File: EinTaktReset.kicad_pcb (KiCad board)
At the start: 2 copper layers, 58 parts, among them IC1 74LS624, J1 3PinTerminalBlocktg, J2 3PinTerminalBlocktg, J3 2PinTerminalBlocktg, J4 3PinTerminalBlocktg, J5 2PinTerminalBlocktg, P1 CONN_02X10, P4 CONN_02X10, SW1 SPST, SW10 SPST, SW11 SPST, SW12 SPST, SW13 SPST, SW2 SWITCH_INV, SW3 SPST, SW4 SPST, SW5 SPST, SW6 SWITCH_INV, SW7 SPST, SW8 SPST, SW9 SPST, U1 74LS132, U2 74540En, U3 74HCT541_PWR, U4 74LS32, U5 74LS00

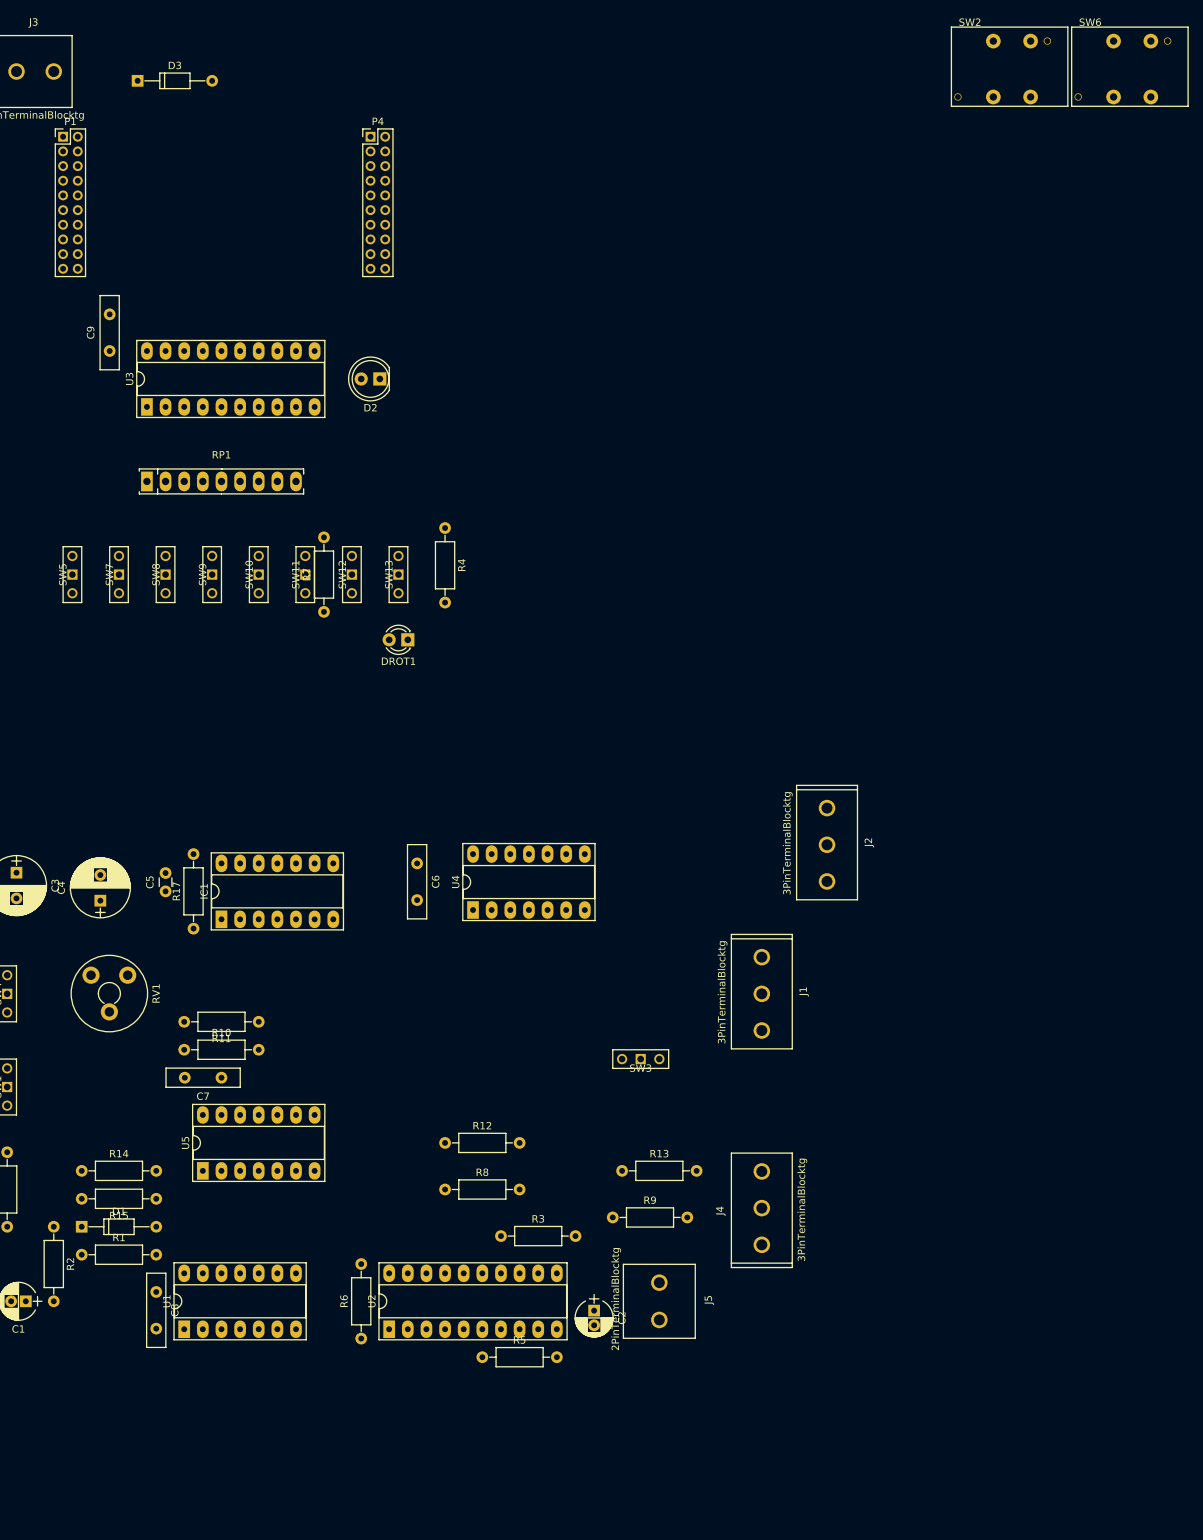
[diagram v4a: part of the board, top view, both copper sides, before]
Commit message: neuer footprint für switch
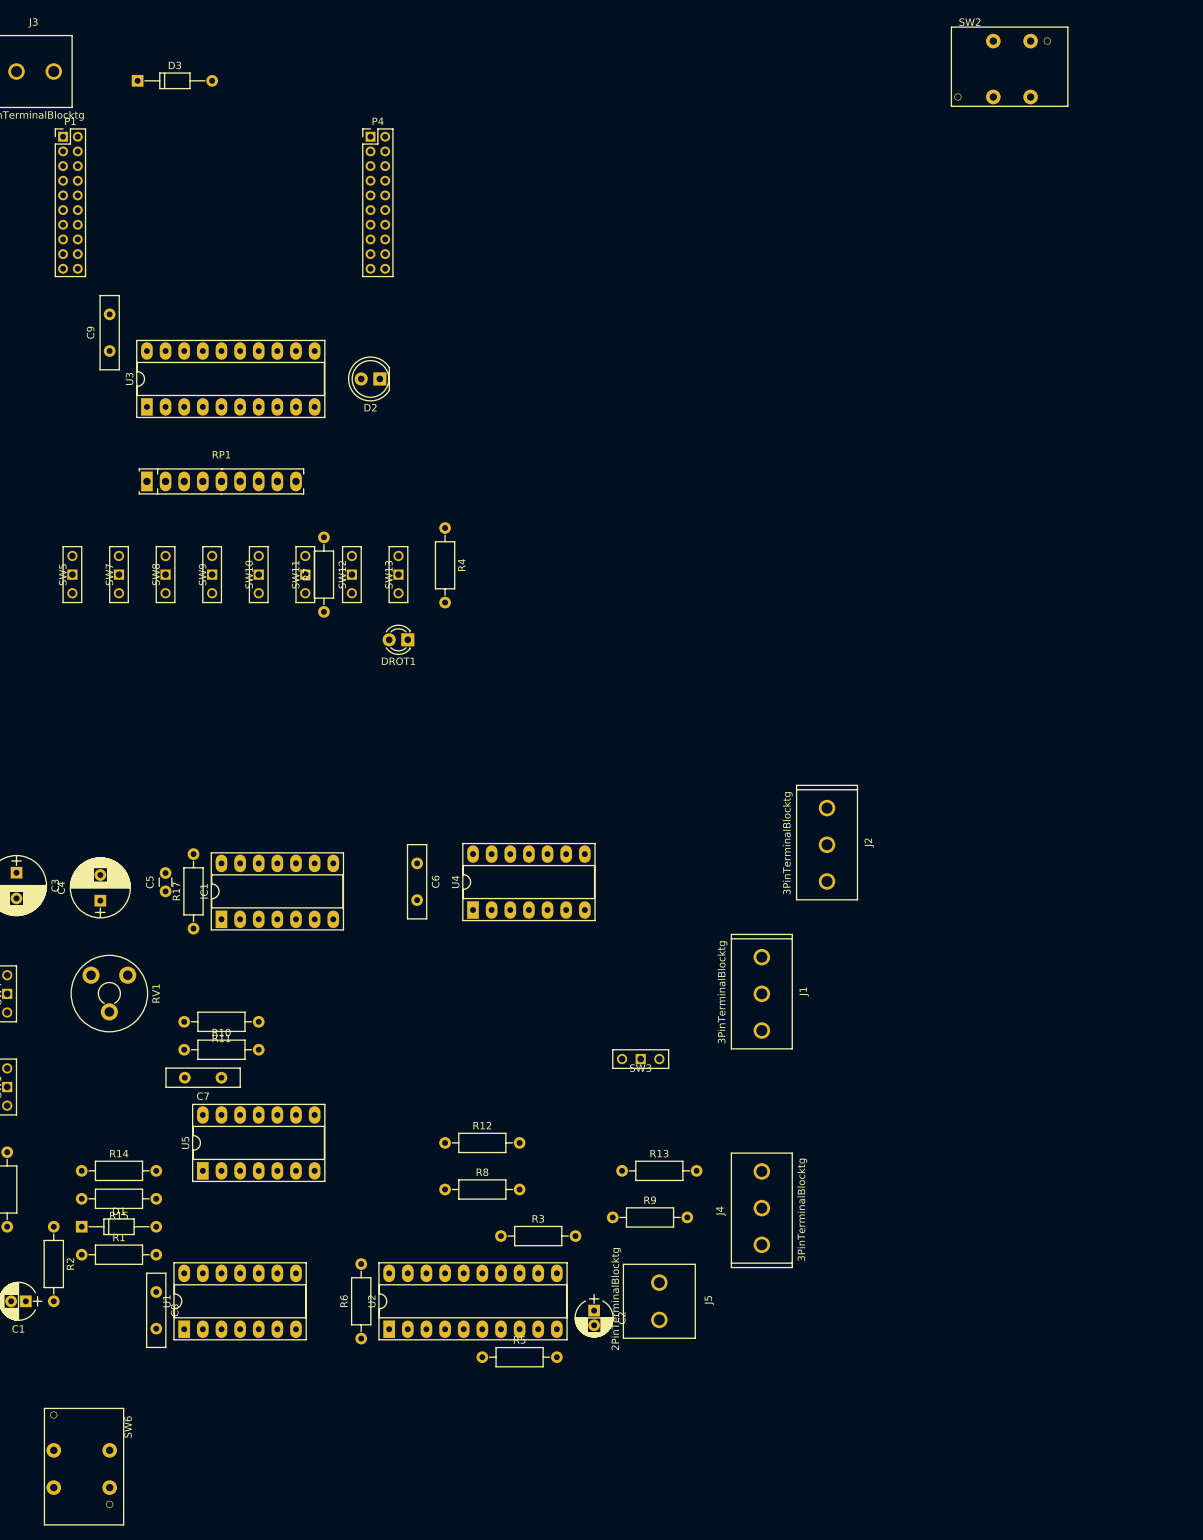
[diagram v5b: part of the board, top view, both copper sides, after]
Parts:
- moved SW6 243.0 mm to (29.2, 210.8), turned to 270 degrees
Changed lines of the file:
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@@
   )
   (module tg_foodprint:SW_PUSH_LCD_E3_SAxxxx_tg (layer F.Cu)
-    (at 171.139157 13.631782)
+    (at 29.21 210.82 270)
     (descr "Switch with LCD screen E3 SAxxxx")
     (tags "switch normally-open pushbutton push-button LCD")
-    (fp_text reference SW6 (at -8.255 -2.54) (layer F.SilkS)
+    (fp_text reference SW6 (at -8.255 -2.54 270) (layer F.SilkS)
       (effects (font (size 1 1) (thickness 0.15)))
     )
@@
       (effects (font (size 1 1) (thickness 0.15)))
     )
-    (fp_text user %R (at -7.5 3.81) (layer F.Fab)
+    (fp_text user %R (at -7.5 3.81 270) (layer F.Fab)
       (effects (font (size 1 1) (thickness 0.15)))
     )
@@
     (fp_line (start 5.08 -1.905) (end -10.795 -1.905) (layer F.Fab) (width 0.1))
     (fp_line (start 5.08 -1.905) (end 5.08 8.89) (layer F.Fab) (width 0.1))
-    (pad 2 thru_hole circle (at 0 7.62) (size 2 2) (drill 1) (layers *.Cu *.Mask)
+    (pad 2 thru_hole circle (at 0 7.62 270) (size 2 2) (drill 1) (layers *.Cu *.Mask)
       (net 11 auto))
-    (pad 0 thru_hole circle (at -5.08 7.62) (size 2 2) (drill 1) (layers *.Cu *.Mask))
-    (pad 1 thru_hole circle (at 0 0) (size 2 2) (drill 1) (layers *.Cu *.Mask)
+    (pad 0 thru_hole circle (at -5.08 7.62 270) (size 2 2) (drill 1) (layers *.Cu *.Mask))
+    (pad 1 thru_hole circle (at 0 0 270) (size 2 2) (drill 1) (layers *.Cu *.Mask)
       (net 12 GND))
-    (pad 5 thru_hole circle (at -9.906 7.62) (size 1 1) (drill 0.8) (layers *.Cu *.Mask))
-    (pad 6 thru_hole circle (at 2.286 0) (size 1 1) (drill 0.8) (layers *.Cu *.Mask))
-    (pad 0 thru_hole circle (at -5.08 0) (size 2 2) (drill 1) (layers *.Cu *.Mask))
+    (pad 5 thru_hole circle (at -9.906 7.62 270) (size 1 1) (drill 0.8) (layers *.Cu *.Mask))
+    (pad 6 thru_hole circle (at 2.286 0 270) (size 1 1) (drill 0.8) (layers *.Cu *.Mask))
+    (pad 0 thru_hole circle (at -5.08 0 270) (size 2 2) (drill 1) (layers *.Cu *.Mask))
     (model ${KISYS3DMOD}/Buttons_Switches_THT.3dshapes/SW_PUSH_LCD_E3_SAxxxx.wrl
       (at (xyz 0 0 0))

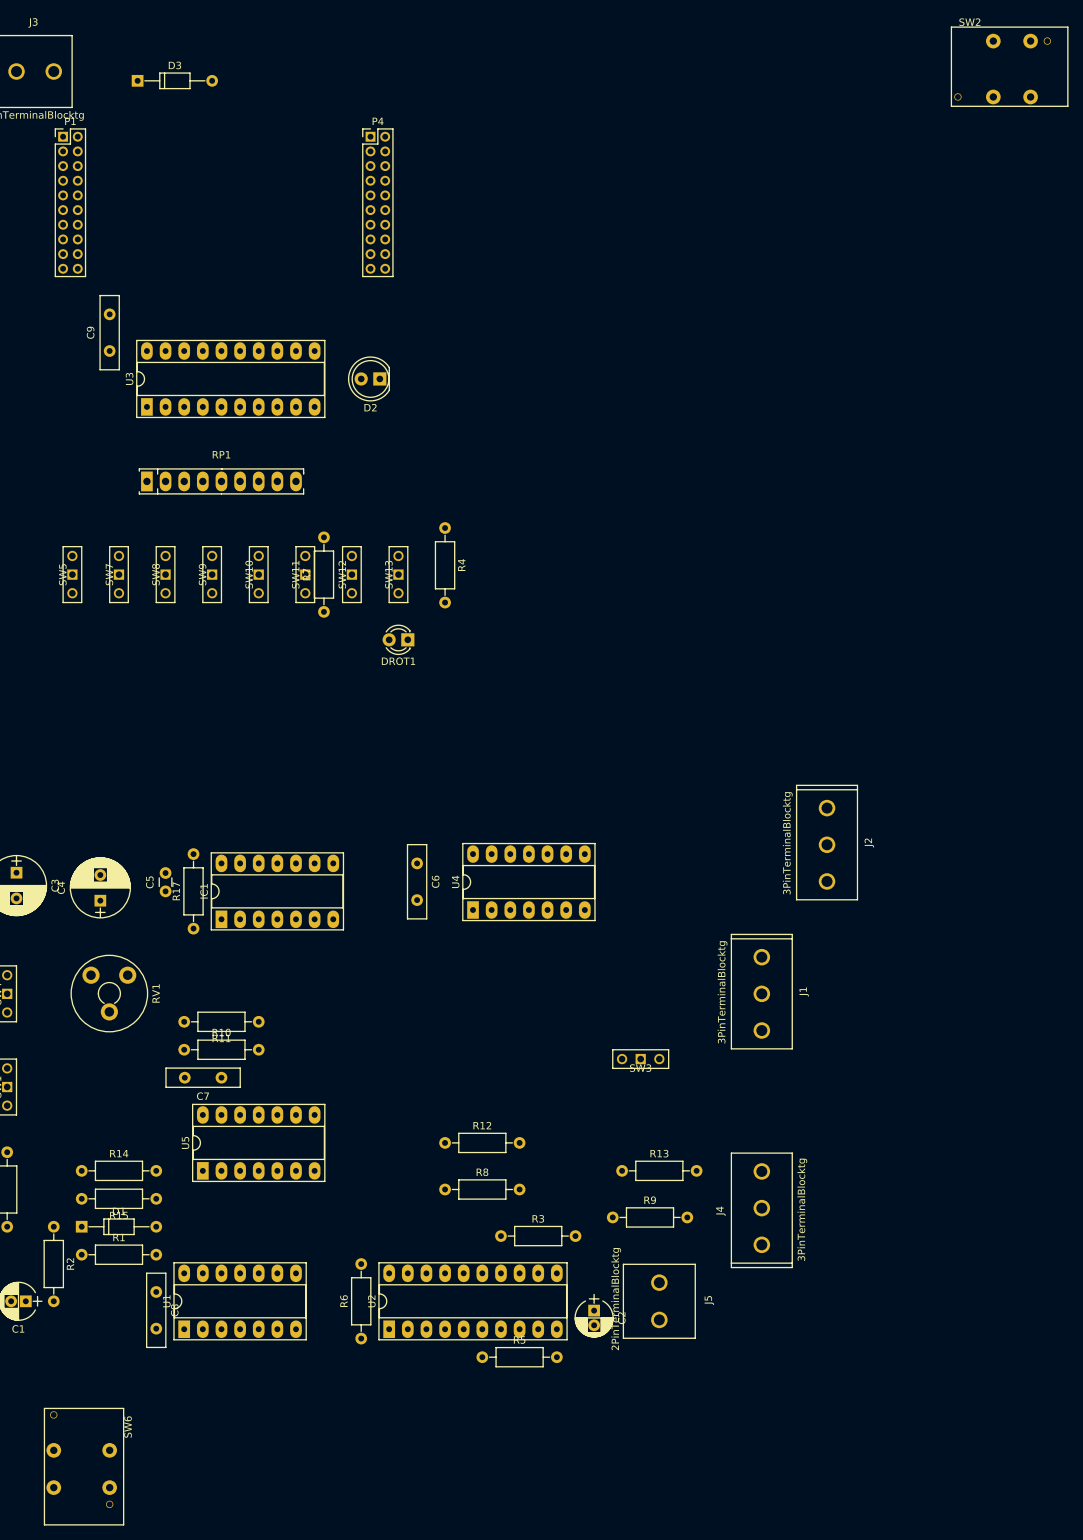
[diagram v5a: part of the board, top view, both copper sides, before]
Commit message: Resistoren angepasst, switches geändert, sw6 braucht noch anpassung
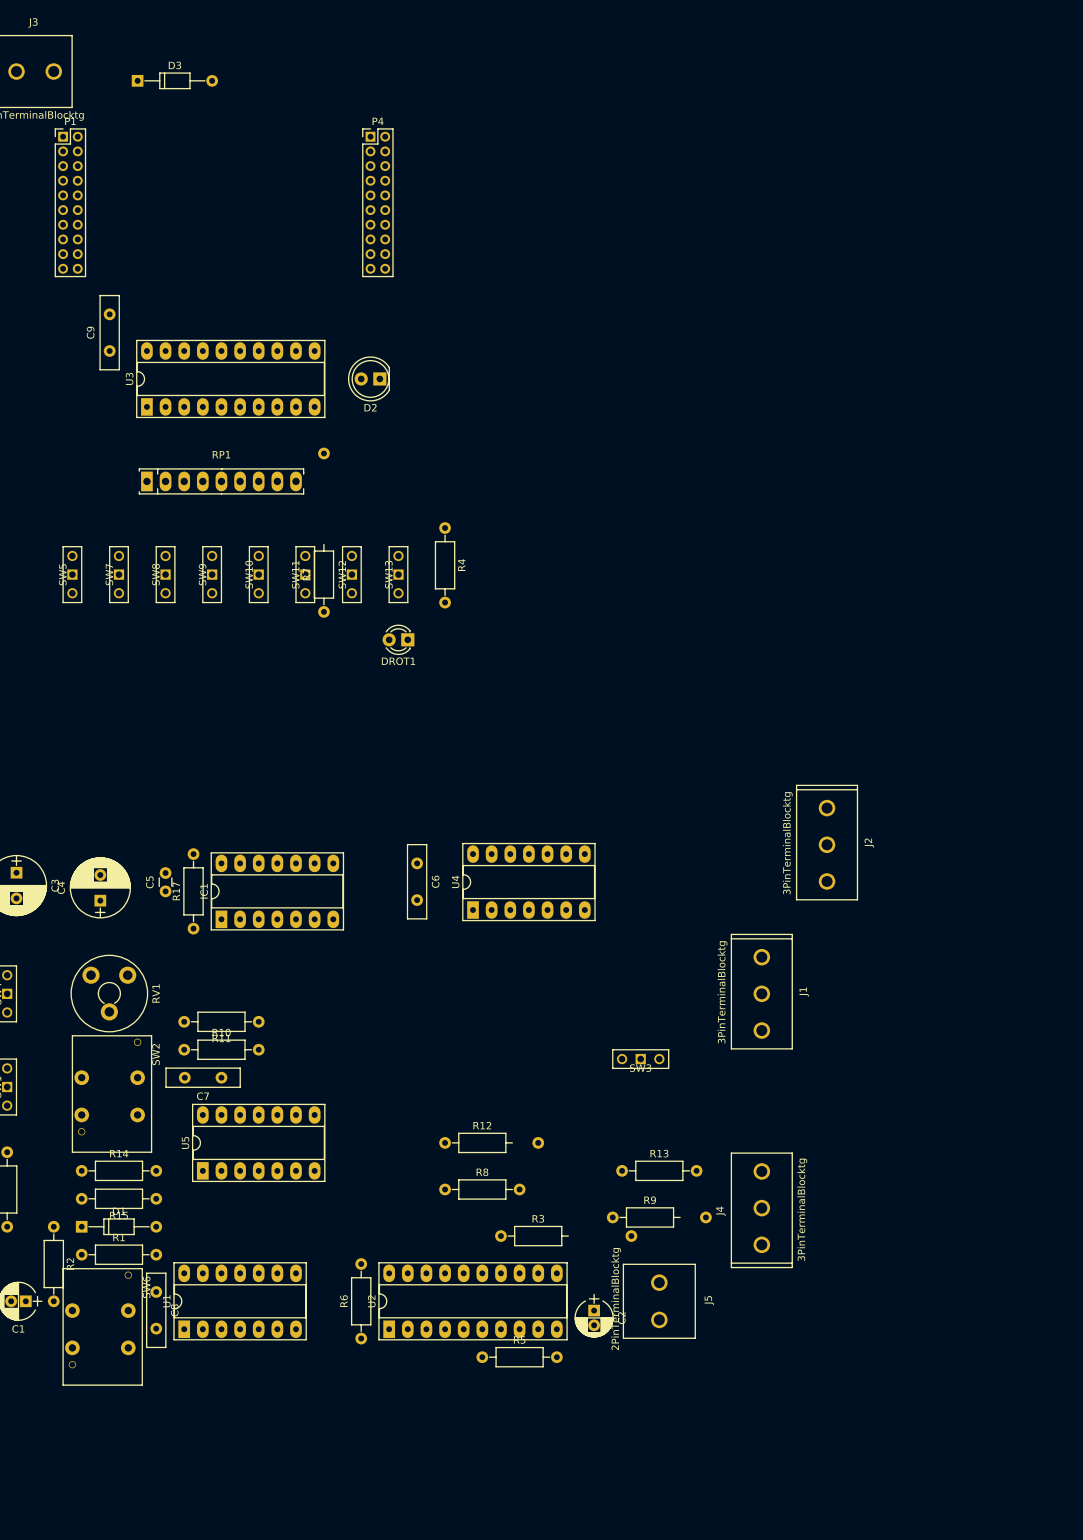
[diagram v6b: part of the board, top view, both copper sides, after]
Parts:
- R12, R9: footprint Resistors_ThroughHole:R_Axial_DIN0207_L6.3mm_D2.5mm_P10.16mm_Horizontal -> tg_foodprint:R_Axial_DIN0207_L6.3mm_D2.5mm_P12.7mm_Horizontaltg
- R3: footprint Resistors_ThroughHole:R_Axial_DIN0207_L6.3mm_D2.5mm_P10.16mm_Horizontal -> tg_foodprint:R_Axial_DIN0207_L6.3mm_D2.5mm_P17.7mm_Horizontaltg
- R7: footprint Resistors_ThroughHole:R_Axial_DIN0207_L6.3mm_D2.5mm_P10.16mm_Horizontal -> tg_foodprint:R_Axial_DIN0207_L6.3mm_D2.5mm_P21.59mm_Horizontaltg
- moved SW2 190.4 mm to (33.0, 160.0), turned to 270 degrees
- moved SW6 19.2 mm to (31.8, 191.8)
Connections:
- SW2 pad 0: (no net) -> GND
- SW2 pad 1: Net-(R14-Pad2) -> Net-(R15-Pad1)
- SW2 pad 2: GND -> Net-(R14-Pad2)
- SW6 pad 0: (no net) -> auto
- SW6 pad 1: GND -> VCC
- SW6 pad 2: auto -> GND

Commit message: eintakt modified
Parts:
- SW1: value SPST -> SWITCH_INV; footprint tg_foodprint:eintakt_tg_SW_CuK_JS202011CQN_DPDT_Straight -> tg_foodprint:SW_PUSH_LCD_E3_SAxxxx_tg
- SW6: footprint tg_foodprint:SW_PUSH_LCD_E3_SAxxxx_tg -> tg_foodprint:eintakt_tg_SW_CuK_JS202011CQN_DPDT_Straight
- moved SW3 89.1 mm to (15.2, 146.1), turned to 270 degrees
- moved SW6 62.7 mm to (82.5, 154.9), turned to 0 degrees
- moved SW1 36.9 mm to (31.8, 191.8), turned to 270 degrees
- moved P1 11.4 mm to (11.4, 26.7)
- moved D1 10.2 mm to (35.6, 175.3), turned to 180 degrees
- moved R1 10.2 mm to (35.6, 179.1), turned to 180 degrees
- moved P4 5.08 mm to (69.8, 26.7)
- moved SW4 3.81 mm to (15.2, 142.2)
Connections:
- SW1 pad 1: GND -> Net-(D1-Pad2)
- SW1 pad 2: Net-(D1-Pad2) -> Net-(SW1-Pad2)
